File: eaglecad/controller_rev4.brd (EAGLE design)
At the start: 160 x 100 mm, 91 parts, among them J1 1.27MM-SWD-CONNECTOR, U101 TCAN330, U200 TPS63070, U300 STSPIN230, U301 TSV991ILT, U302 AS5047P, U400 STSPIN250, U401 TSV991ILT, X101 16MHZ-2.5x2mm

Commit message: F4 updates
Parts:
- added C107: 2.2u, rcl_custom:.0402-B-NOSILK
- moved U$1 55.5 mm to (24.9, 24.4), turned to 180 degrees
- moved JP301 20.0 mm to (2.33, 33.5), turned to 90 degrees
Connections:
- new net N$6: C107.2, U$1.P$30
- net GND: now also C107.1
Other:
- board size 160 x 100 mm -> 40 x 39.5 mm

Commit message: F4 uPdateS
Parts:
- added C304, C404: 1n, rcl_custom:.0402-B-NOSILK
- added R301, R401: 18k, rcl_custom:.0402-B-NOSILK
- moved C107 164.4 mm to (37.0, 129.5)
- moved X101 143.5 mm to (48.0, 114.0), turned to 270 degrees
- moved R303 134.1 mm to (-11.2, 152.7)
- moved U300 132.4 mm to (9.93, 122.1)
- moved C103 130.5 mm to (49.0, 121.0), turned to 90 degrees
- moved R409 130.2 mm to (69.0, 55.0)
- moved R408 128.9 mm to (71.5, 54.5), turned to 270 degrees
- moved C102 126.4 mm to (48.0, 121.0), turned to 90 degrees
- moved R406 124.5 mm to (73.0, 69.0)
- moved R407 124.1 mm to (70.5, 54.5), turned to 270 degrees
- moved C101 122.5 mm to (47.0, 121.0), turned to 90 degrees
- moved C407 122.4 mm to (69.0, 53.0)
- moved R405 120.9 mm to (73.0, 70.0)
- moved C406 120.5 mm to (71.0, 53.0), turned to 180 degrees
- moved J1 118.5 mm to (61.5, 98.1), turned to 180 degrees
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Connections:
- net 3.3V: now also R301.1, R401.1
- net GND: now also C304.1, C404.1
- net STBY/RESET_BLDC: now also C304.2, R301.2
- net STBY/RESET_MAG: now also C404.2, R401.2
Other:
- board size 40 x 39.5 mm -> 40 x 29.5 mm

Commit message: F4 updates
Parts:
- moved C310 117.9 mm to (19.2, 15.2)
- moved R301 117.8 mm to (20.4, 17.4), turned to 90 degrees
- moved C304 114.7 mm to (19.1, 17.4), turned to 90 degrees
- moved R315 113.1 mm to (20.0, 22.5), flipped to the bottom, turned to 270 degrees
- moved U300 104.2 mm to (15.9, 18.1), turned to 270 degrees
- moved C105 99.5 mm to (37.8, 17.1)
- moved C104 99.5 mm to (37.9, 12.8)
- moved X101 99.5 mm to (37.9, 15.0)
- moved JP401 90.6 mm to (29.4, 70.2), turned to 180 degrees
- moved JP103 90.4 mm to (46.2, 18.8), turned to 90 degrees
- moved R310 48.4 mm to (-22.3, 101.9), turned to 270 degrees
- moved R311 45.1 mm to (-24.3, 101.9), turned to 270 degrees
- moved C306 44.1 mm to (-20.8, 101.5), turned to 90 degrees
- moved C307 41.2 mm to (-19.3, 105.0), turned to 0 degrees
- moved R314 34.2 mm to (-16.7, 101.5), turned to 270 degrees
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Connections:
- net PA0/CURR_FDB_MAG renamed MAG_CURR_FDB
- net PA1/CURR_FDB_BLDC renamed BLDC_CURR_FDB
- net PA10/INWH renamed BLDC_INWH
- net PA15/CAN_SILENT renamed CAN_SILENT
- net PA2/USART2_TX renamed USART2_TX
- net PA3/USART2_RX renamed USART2_RX
- net PA4/FAULT_BLDC renamed BLDC_FAULT
- net PA5/SPI1_SCK renamed SPI1_SCK
- net PA6/SPI1_NSS renamed SPI1_NSS
- net PA7/INUL renamed BLDC_INUL
- net PB0/INVL renamed BLDC_INVL
- net PB1/INWL renamed BLDC_INWL
- net PB3/EN_MAG renamed MAG_EN
- net PB4/SPI1_MISO renamed SPI1_MISO
- net PB6/EN_BLDC renamed BLDC_EN
- net PB7/FAULT_MAG renamed MAG_FAULT
- removed net PA8/INUH/PWM_MAG: R406.2, U$1.P$41, U300.2
- removed net PA9/INVH/DIR_MAG: R405.2, U$1.P$42, U300.16
- removed net STBY/RESET_BLDC: C304.2, R301.2, TP2.TP, U300.14
- removed net STBY/RESET_MAG: C404.2, R401.2, TP3.TP, U400.14
- new net BLDC_INUH: U$1.P$41, U300.2
- new net BLDC_INVH: U$1.P$42, U300.16
- new net BLDC_STBY: C304.2, R301.2, TP2.TP, U$1.P$39, U300.14
- new net MAG_DIR: R405.2, U$1.P$57
- new net MAG_PWM: R406.2, U$1.P$56
- new net MAG_STBY: C404.2, R401.2, TP3.TP, U$1.P$58, U400.14
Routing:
- net SPI1_NSS: track 0.00 -> 18.9 mm, vias 0 -> 1
- net SPI1_SCK: track 0.00 -> 17.4 mm, vias 0 -> 1
- net SPI1_MISO: track 0.00 -> 16.2 mm, vias 0 -> 1
- net BLDC_INUH: track 0.00 -> 10.8 mm
- net BLDC_INWL: track 0.00 -> 10.3 mm, vias 0 -> 2
- net BLDC_INWH: track 0.00 -> 8.94 mm
- net BLDC_INVH: track 0.00 -> 8.91 mm
- net BLDC_INUL: track 0.00 -> 7.75 mm, vias 0 -> 2
- net BLDC_INVL: track 0.00 -> 7.32 mm, vias 0 -> 2
- net BLDC_FAULT: track 0.00 -> 7.11 mm, vias 0 -> 2
- net 3.3V: track 0.00 -> 4.07 mm, vias 0 -> 1
- net BLDC_STBY: track 0.00 -> 3.16 mm
- net GND: track 0.00 -> 2.77 mm, vias 0 -> 1
- net CAN_TX: track 0.00 -> 2.22 mm
- net AS5047_MOSI: track 0.00 -> 1.06 mm

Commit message: F4 update
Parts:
- removed 3.3V, EN, FB2, PG, VSEL: TPTP15SQ, testpad:TP15SQ
- removed C201, C202: 10u, oresat-rcl:.0805-B-NOSILK
- removed C203: 10u, oresat-rcl:.0603-B-NOSILK
- removed C204: 100n, rcl_custom:.0402-B-NOSILK
- removed C205: 22u, oresat-rcl:.0603-B-NOSILK
- removed C206, C207: 22u, oresat-rcl:.0805-B-NOSILK
- removed L201: 1.5 uH, L-Coilcraft-XFL4020:L-COILCRAFT-XFL4020
- removed R201: 0, rcl_custom:.0805-B-NOSILK
- removed R202, R204: 10k, rcl_custom:.0402-B-NOSILK
- removed R203, R207: NP, rcl_custom:.0402-B-NOSILK
- removed R205: 470k, rcl_custom:.0402-B-NOSILK
- removed R206: 150k, rcl_custom:.0402-B-NOSILK
- removed U200: TPS63070, ic-pwr-tps63070x:TPS63070X
- added C1: 10u, oresat-rcl:.0603-B-NOSILK
- added C10, C11: 22u, oresat-rcl:.0805-B-NOSILK
- added C2: 100n, rcl_custom:.0402-B-NOSILK
- added C3, C7: 10u, oresat-rcl:.0805-B-NOSILK
- added C9: 22u, oresat-rcl:.0603-B-NOSILK
- added L1: 1.5 uH, L-Coilcraft-XFL4020:L-COILCRAFT-XFL4020
- added R1, R4: 10k, rcl_custom:.0402-B-NOSILK
- added R2: 470k, rcl_custom:.0402-B-NOSILK
- added R3: 150k, rcl_custom:.0402-B-NOSILK
- added R6: NP, rcl_custom:.0402-B-NOSILK
- added U2: TPS63070, ic-pwr-tps63070x:TPS63070X
- moved R303 136.8 mm to (4.73, 16.8), turned to 90 degrees
- moved C305 117.6 mm to (23.1, 16.2), flipped to the bottom, turned to 90 degrees
- moved R101 116.2 mm to (31.3, 14.8), flipped to the bottom, turned to 270 degrees
- moved C103 112.2 mm to (34.1, 9.80), turned to 0 degrees
- moved C107 107.2 mm to (27.7, 22.7), flipped to the bottom
- moved R302 105.0 mm to (22.6, 17.9), turned to 90 degrees
- moved C101 100.9 mm to (24.9, 22.6), turned to 0 degrees
- moved BOOT 99.2 mm to (30.9, 12.8), flipped to the bottom
- moved JP301 99.1 mm to (1.67, 23.5)
- moved C102 98.4 mm to (33.3, 23.7), turned to 180 degrees
- moved C303 93.8 mm to (6.50, 17.0), turned to 270 degrees
- moved C302 92.7 mm to (8.00, 17.0), turned to 270 degrees
- moved C301 91.7 mm to (9.50, 17.0), turned to 270 degrees
- moved TP3 87.5 mm to (16.4, -10.6)
- moved R311 86.7 mm to (11.9, 23.1), flipped to the bottom, turned to 0 degrees
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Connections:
- removed net TPS-EN: EN.TP, R202.1, R203.2, U200.1, U200.14
- removed net TPS-FB: R205.1, R206.2, U200.5
- removed net TPS-L1: L201.1, U200.11
- removed net TPS-L2: L201.2, U200.9
- removed net TPS-PG: PG.TP, R207.1, U200.2
- removed net TPS-VAUX: C204.1, U200.3
- removed net TPS-VIN: C201.1, C202.1, C203.1, R201.1, R202.2, U200.12-13
- removed net TSP-FB2: FB2.TP, U200.6
- removed net TSP-VSEL: R204.2, U200.15, VSEL.TP
- new net TPS-EN2: R1.1, R6.2, U2.1, U2.14
- new net TPS-FB2: R2.1, R3.2, U2.5
- new net TPS-L5: L1.1, U2.11
- new net TPS-L6: L1.2, U2.9
- new net TPS-VAUX2: C2.1, U2.3
- new net TPS-VSEL2: R4.2, U2.15
- new net VBUS: C1.1, C3.1, C7.1, R1.2, U2.12-13
- net 3.3V: now also C10.1, C11.1, C9.1, R2.2, U2.7-8; no longer 3.3V.TP, C205.1, C206.1, C207.1, R205.2, R207.2, U200.7-8
- net GND: now also C1.2, C10.2, C11.2, C2.2, C3.2, C7.2, C9.2, R3.1, R4.1, R6.1, U2.10, U2.4; no longer C201.2, C202.2, C203.2, C204.2, C205.2, C206.2, C207.2, R203.1, R204.1, R206.1, U200.10, U200.4
- net V_BATT: no longer R201.2
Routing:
- net BLDC_STBY: track 3.16 -> 11.9 mm, vias 0 -> 2
- net TPS-L6: track 0.00 -> 6.60 mm, vias 0 -> 7
- net TPS-L5: track 0.00 -> 6.60 mm, vias 0 -> 7
- net BLDC_FAULT: track 7.11 -> 12.0 mm
- net TPS-EN2: track 0.00 -> 4.53 mm
- net GND: track 2.77 -> 7.23 mm, vias 1 -> 14
- net TPS-FB2: track 0.00 -> 2.50 mm
- net CAN_TX: track 2.22 -> 0.00 mm
- net BLDC_EN: track 0.00 -> 1.55 mm
- net VBUS: track 0.00 -> 1.50 mm
- net TPS-VSEL2: track 0.00 -> 1.35 mm
- added copper zone on layer 1, net 3.3V
- added copper zone on layer 1, net TPS-L5
- added copper zone on layer 1, net TPS-L6
- added copper zone on layer 1, net VBUS
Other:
- board text added: "3.3V"
- board text added: "Vin"

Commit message: L4 updates
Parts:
- U$1: value STM32F446X -> STM32L452XX_QFPN48; device oresat-misc:LQFP_64-HIGH_DENSITY -> oresat-ACS_driver_board:QFPN-48
- moved C106 111.3 mm to (22.9, 13.0), turned to 270 degrees
- moved TP2 91.0 mm to (18.5, 35.4)
- moved JP1 76.7 mm to (23.2, -2.22)
- moved J1 73.0 mm to (44.5, 27.1)
- moved TP1 64.0 mm to (13.6, 33.6)
- moved C403 61.3 mm to (15.7, 5.30), turned to 180 degrees
- moved C402 59.4 mm to (15.7, 6.80), turned to 180 degrees
- moved C401 57.4 mm to (15.7, 8.30), turned to 180 degrees
- moved JP102 45.6 mm to (9.25, -2.22)
- moved JP103 9.22 mm to (44.2, 9.82)
- moved TP3 7.00 mm to (16.4, -3.58)
- moved C11 3.71 mm to (11.3, 9.30), turned to 270 degrees
- moved U$1 2.17 mm to (32.0, 17.0)
- moved R2 1.77 mm to (9.30, 10.1)
- moved R405 1.70 mm to (30.3, 9.00)
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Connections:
- net 3.3V: no longer U$1.P$1, U$1.P$13, U$1.P$19, U$1.P$32, U$1.P$48, U$1.P$64
- net BLDC_CURR_FDB: now also U$1.11; no longer U$1.P$17
- net BLDC_EN: now also U$1.33; no longer U$1.P$37
- net BLDC_FAULT: now also U$1.32; no longer U$1.P$38
- net BLDC_INUH: now also U$1.26; no longer U$1.P$41
- net BLDC_INUL: now also U$1.29; no longer U$1.P$34
- net BLDC_INVH: now also U$1.27; no longer U$1.P$42
- net BLDC_INVL: now also U$1.30; no longer U$1.P$35
- net BLDC_INWH: now also U$1.28; no longer U$1.P$43
- net BLDC_INWL: now also U$1.31; no longer U$1.P$36
- net BLDC_STBY: now also U$1.25; no longer U$1.P$39
- net BOOT: no longer U$1.P$60
- net CAN_RX: no longer U$1.P$44
- net CAN_SILENT: no longer U$1.P$50
- net CAN_TX: no longer U$1.P$45
- net GND: no longer U$1.P$12, U$1.P$18, U$1.P$31, U$1.P$47, U$1.P$63
- net MAG_CURR_FDB: now also U$1.10; no longer U$1.P$16
- net MAG_DIR: now also U$1.39; no longer U$1.P$57
- net MAG_EN: now also U$1.46; no longer U$1.P$62
- net MAG_FAULT: now also U$1.45; no longer U$1.P$61
- net MAG_PWM: now also U$1.38; no longer U$1.P$56
- net MAG_STBY: now also U$1.43; no longer U$1.P$58
- net N$1: no longer U$1.P$5
- net N$4: no longer U$1.P$6
- net N$6: no longer U$1.P$30
- net NRESET: no longer U$1.P$7
- net SPI1_MISO: now also U$1.16; no longer U$1.P$22
- net SPI1_NSS: now also U$1.14; no longer U$1.P$20
- net SPI1_SCK: now also U$1.15; no longer U$1.P$21
- net SWCLK: no longer U$1.P$49
- net SWDIO: no longer U$1.P$46
- net USART2_RX: no longer U$1.P$15
- net USART2_TX: no longer U$1.P$14
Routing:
- net SENSE_MAG: track 0.00 -> 3.22 mm
- net MAG-I-IN+: track 0.00 -> 3.16 mm
- net CAN_RX: track 0.00 -> 3.14 mm
- net BLDC_INWH: track 8.94 -> 5.88 mm
- net MAG-I-IN-: track 0.00 -> 2.88 mm
- net 3.3V: track 4.07 -> 6.27 mm
- net BLDC_INUL: track 7.75 -> 5.59 mm
- net MAG-I-OUT: track 0.00 -> 2.15 mm
- net BLDC_INVH: track 9.24 -> 7.12 mm
- net BLDC_INUH: track 10.8 -> 8.69 mm
- net CAN_TX: track 0.00 -> 1.76 mm
- net BLDC_FAULT: track 12.0 -> 10.3 mm
- net BLDC_INVL: track 7.40 -> 5.74 mm
- net BLDC_INWL: track 10.4 -> 8.97 mm
- net SPI1_MISO: track 16.2 -> 14.9 mm
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
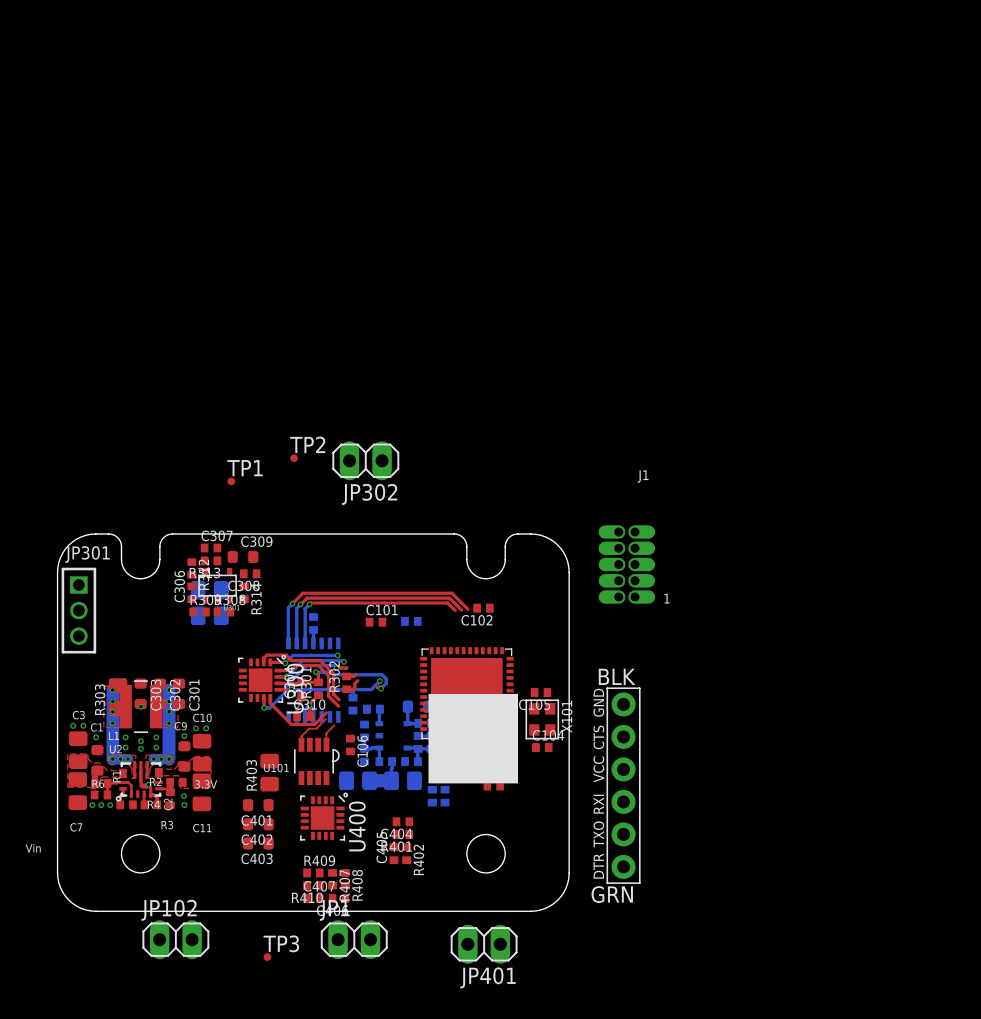
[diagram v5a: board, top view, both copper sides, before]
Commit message: Schematic Overhal and chip opperation verification
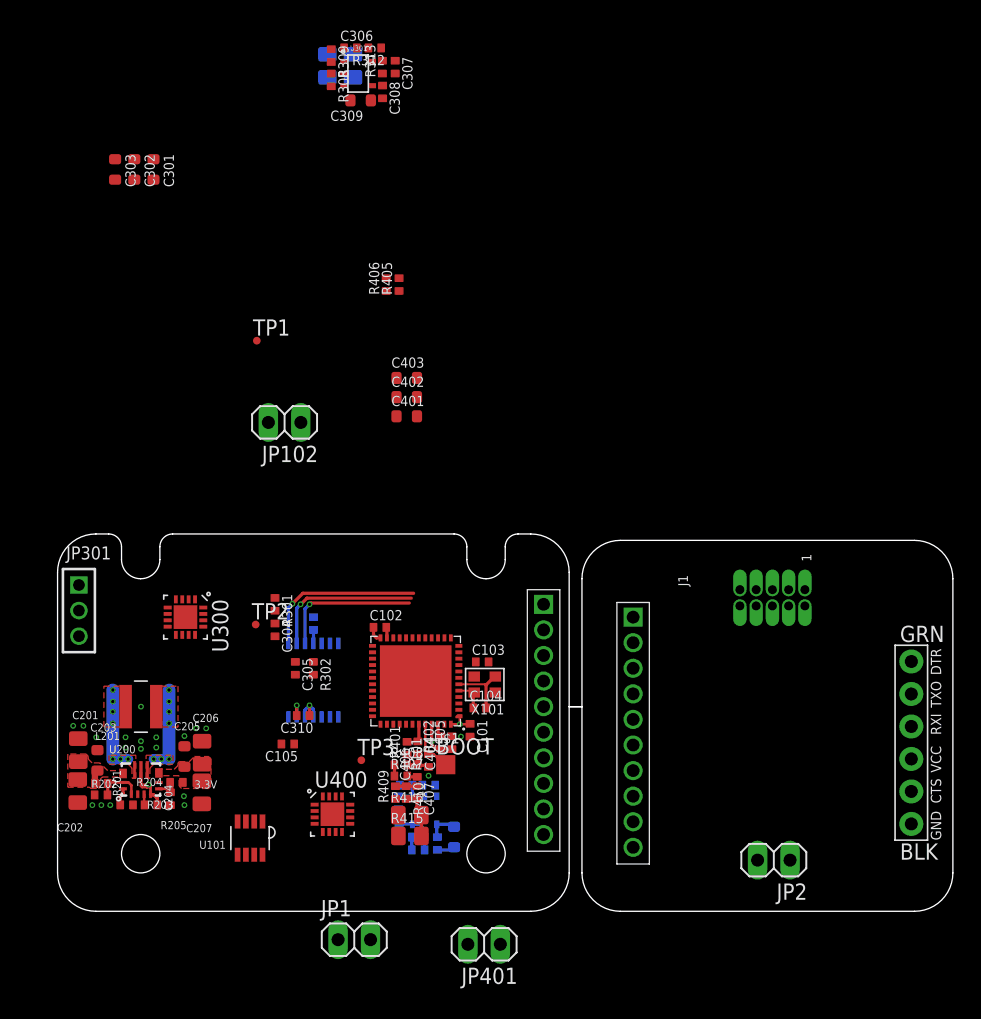
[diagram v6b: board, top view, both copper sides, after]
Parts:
- removed C106: 100n, rcl_custom:.0402-B-NOSILK
- removed C107: 2.2u, rcl_custom:.0402-B-NOSILK
- removed JP302: (no value), pinhead:1X02
- removed R303, R403: 0, oresat-rcl:.0805-B-NOSILK
- removed R314, R419: 0, rcl_custom:.0402-B-NOSILK
- added JP2: (no value), pinhead:1X02
- added U$2, U$3: DEBUG_CON, oresat-ACS_driver_board:DEBUG_CON
- C103: value 100n -> 10n
- C104: value 20p -> 10p
- C105: value 20p -> 100n
- U300: device U-ST-STSPIN230-BLDC-controller:VFQFPN -> oresat-ACS_driver_board:VFQPN
- U301, U401: device TSV991ILT:SOT23-5 -> oresat-ACS_driver_board:SOT23-5
- U400: device U-ST-STSPIN250-Brushed-DC-controller:VFQPN -> oresat-ACS_driver_board:VFQPN
- X101: value 16MHZ-2.5x2mm -> ABM10-16MHz
- moved R309 44.7 mm to (21.4, 66.9), turned to 270 degrees
- moved C306 44.4 mm to (22.9, 67.5), turned to 0 degrees
- moved R311 44.0 mm to (21.1, 66.1), turned to 90 degrees
- moved R312 43.1 mm to (24.8, 67.5), turned to 180 degrees
- moved R310 42.5 mm to (23.1, 66.1), turned to 90 degrees
- moved R308 42.4 mm to (21.4, 65.0), turned to 270 degrees
- moved U301 41.5 mm to (23.5, 65.5), turned to 0 degrees
- moved JP102 41.3 mm to (17.8, 38.2), turned to 180 degrees
- moved C301 41.0 mm to (7.50, 58.0)
- moved C302 41.0 mm to (6.00, 58.0)
- moved C303 41.0 mm to (4.50, 58.0)
- moved R313 40.9 mm to (25.4, 66.0), turned to 90 degrees
- moved C307 40.3 mm to (26.4, 66.0), turned to 270 degrees
- moved R405 40.2 mm to (26.7, 49.0), flipped to the top
- moved R406 40.2 mm to (25.7, 49.0), flipped to the top
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- renumbered C1 to C203, C10 to C206, C11 to C207, C2 to C204, C3 to C201, C7 to C202, C9 to C205, L1 to L201, R1 to R201, R2 to R204, R3 to R205, R4 to R203, R6 to R202, U2 to U200
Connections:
- net NRESET renamed NRESET_D
- net USART2_RX renamed USART_RX_D
- net USART2_TX renamed USART_TX_D
- removed net BLDC-I-IN+: C306.1, R308.1, R309.2, U301.IN+
- removed net BLDC-I-IN-: C307.1, R312.1, R313.2, U301.IN-
- removed net BLDC-I-OUT: C307.2, R313.1, R314.2, U301.OUT
- removed net MAG-I-IN+: C408.1, R413.1, R414.2, U401.IN+
- removed net MAG-I-IN-: C411.1, R417.1, R418.2, U401.IN-
- removed net MAG-I-OUT: C411.2, R418.1, R419.2, U401.OUT
- removed net N$6: C107.2
- removed net N$8: C401.1, C402.1, C403.1, R403.1, U400.6
- new net N$11: C411.2, R417.2, R418.1, U401.5
- new net N$12: C307.2, R312.2, R313.1, U301.5
- new net N$9: C306.1, R308.1, R309.2, U301.1
- new net NRST: U$1.7
- new net QUAD_A_D: JP2.1
- new net QUAD_B_D: JP2.2
- new net SWCLK_D: J1.SWDCLK
- new net SWDIO_D: J1.SWDIO
- new net UART_RX: U$1.13
- new net UART_XT: U$1.12
- net 250_REF: now also C407.1; no longer C407.2
- net 3.3V: now also C101.1, C102.1, C103.1, C105.2, C308.1, C310.1, U$1.1, U$1.24, U$1.48, U$1.9, U$2.2, U$3.2, U301.4, U401.4; no longer C101.2, C102.2, C103.2, C106.2, C308.2, C310.2, U301.VCC+, U401.VCC+
- net BLDC_CURR_FDB: now also C307.1, R313.2, U301.3; no longer R314.1
- net BLDC_FAULT: now also C305.1; no longer C305.2
- net BLDC_STBY: now also C304.1; no longer C304.2
- net BOOT: now also U$1.44
- net CAN_RX: now also U$1.41
- net CAN_SILENT: now also U$1.40
- net CAN_TX: now also U$1.42
- net GND: now also C101.2, C102.2, C103.2, C304.2, C305.2, C308.2, C310.2, C404.2, C405.2, C406.2, C407.2, R312.1, R417.1, U$1.23, U$1.35, U$1.36, U$1.47, U$1.8, U$1.EPAD, U$2.10, U$3.10, U301.2, U401.2; no longer C101.1, C102.1, C103.1, C104.1, C106.1, C107.1, C304.1, C305.1, C308.1, C310.1, C404.1, C405.1, C406.1, C407.1, R312.2, R417.2, U301.VCC-, U401.VCC-
- net MAG_CURR_FDB: now also C411.1, R418.2, U401.3; no longer R419.1
- net MAG_FAULT: now also C405.1; no longer C405.2
- net MAG_STBY: now also C404.1; no longer C404.2
- net N$1: now also U$1.6, X101.1; no longer X101.3
- net N$2: now also C406.1; no longer C406.2
- net N$4: now also C104.1, U$1.5, X101.3; no longer C105.2, X101.1
- net N$7: now also C408.1, R413.1, R414.2, U401.1; no longer C301.1, C302.1, C303.1, R303.1, U300.6
- net QUAD_A: no longer JP302.1
- net QUAD_B: no longer JP302.2
- net SWCLK: now also U$1.37; no longer J1.SWDCLK
- net SWDIO: now also U$1.34; no longer J1.SWDIO
- net VBUS: now also C301.1, C302.1, C303.1, C401.1, C402.1, C403.1, JP1.1, JP103.P$4, U$3.1, U300.6, U400.6
- net V_BATT: now also U$2.1; no longer JP1.1, JP103.P$4, R303.2, R403.2
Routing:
- net BLDC_STBY: track 11.0 -> 0.00 mm, vias 2 -> 0
- net BLDC_FAULT: track 10.3 -> 0.00 mm, vias 2 -> 0
- net BLDC_INWL: track 8.97 -> 0.00 mm, vias 2 -> 0
- net BLDC_INUH: track 8.69 -> 0.00 mm
- net GND: track 7.23 -> 14.8 mm, vias 20 -> 22
- net BLDC_INVH: track 7.12 -> 0.00 mm
- net BLDC_INWH: track 5.88 -> 0.00 mm
- net BLDC_INVL: track 5.74 -> 0.00 mm, vias 2 -> 0
- net BLDC_INUL: track 5.59 -> 0.00 mm, vias 2 -> 0
- net N$1: track 0.00 -> 4.94 mm
- net SPI1_NSS: track 17.8 -> 13.0 mm
- net BOOT: track 0.00 -> 4.61 mm
- net SPI1_SCK: track 16.4 -> 12.0 mm
- net SPI1_MISO: track 14.9 -> 11.0 mm
- net N$11: track 0.00 -> 3.77 mm
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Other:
- board size 40 x 29.5 mm -> 70 x 29.5 mm
- board text removed: "Vin"
